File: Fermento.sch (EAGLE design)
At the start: 27 parts, among them Q1 32.768kHz, Q2 P-MOSFET

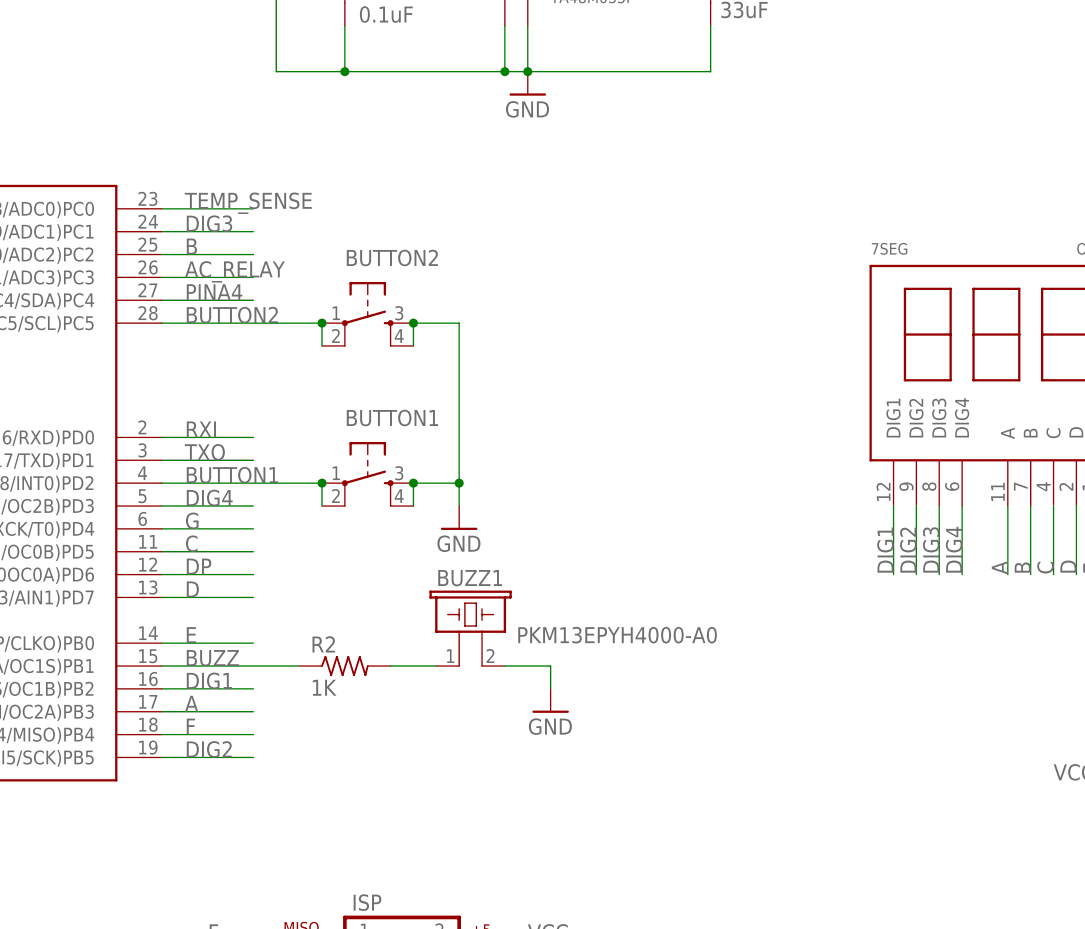
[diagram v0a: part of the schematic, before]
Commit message: Added firmware to the repo.
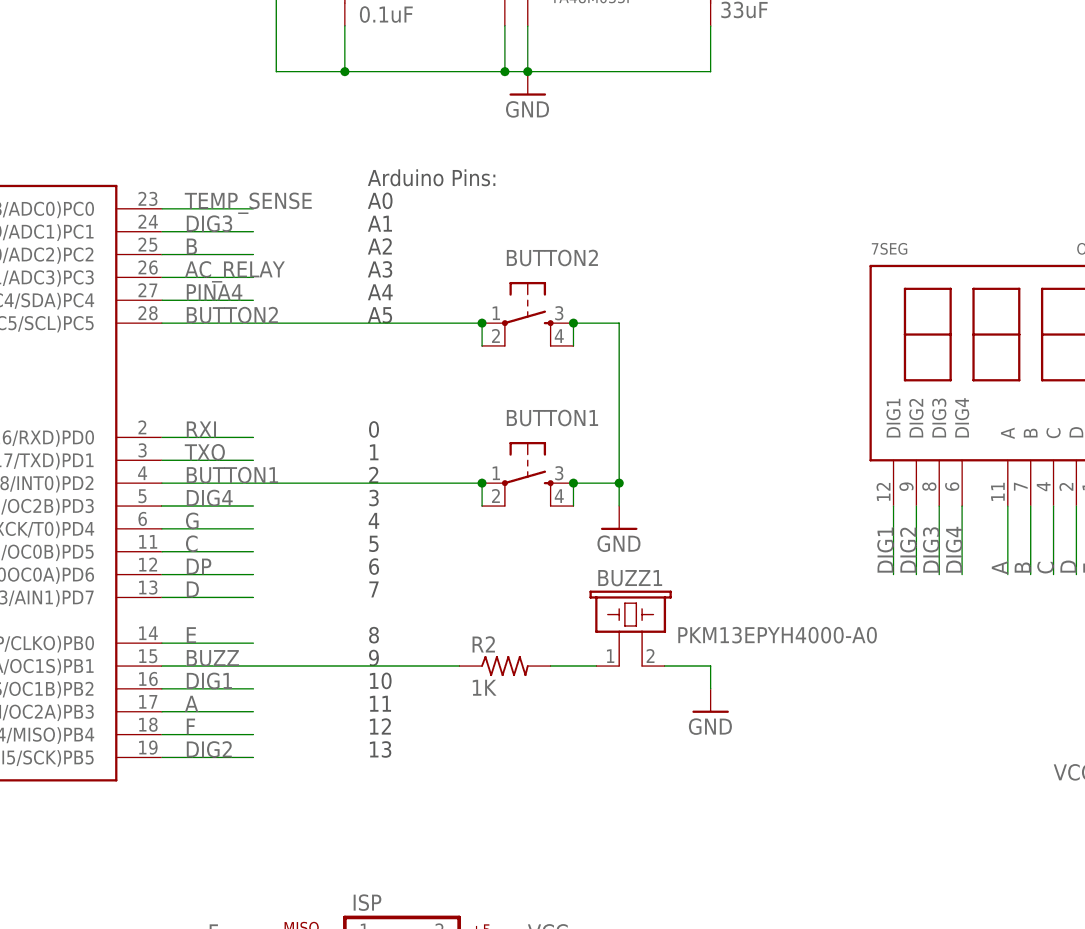
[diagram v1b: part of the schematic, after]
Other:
- note added: "0"
- note added: "1"
- note added: "10"
- note added: "11"
- note added: "12"
- note added: "13"
- note added: "3"
- note added: "4"
- note added: "5"
- note added: "6"
- note added: "7"
- note added: "8"
- note added: "9"
- note added: "A0"
- note added: "A1"
- note added: "A2"
- note added: "A3"
- note added: "A4"
- note added: "A5"
- note added: "Arduino Pins:"
- moved on the sheet: BUTTON1, BUTTON2, BUZZ1, R2
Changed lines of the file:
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@@
 <text x="259.08" y="-198.12" size="2.286" layer="94">2</text>
 <text x="190.5" y="-198.12" size="2.286" layer="94">based on BigTime by SparkFun</text>
+<text x="137.16" y="-81.28" size="1.778" layer="97">0</text>
+<text x="137.16" y="-83.82" size="1.778" layer="97">1</text>
+<text x="137.16" y="-86.36" size="1.778" layer="97">2</text>
+<text x="137.16" y="-88.9" size="1.778" layer="97">3</text>
+<text x="137.16" y="-91.44" size="1.778" layer="97">4</text>
+<text x="137.16" y="-93.98" size="1.778" layer="97">5</text>
+<text x="137.16" y="-96.52" size="1.778" layer="97">6</text>
+<text x="137.16" y="-99.06" size="1.778" layer="97">7</text>
+<text x="137.16" y="-104.14" size="1.778" layer="97">8</text>
+<text x="137.16" y="-106.68" size="1.778" layer="97">9</text>
+<text x="137.16" y="-109.22" size="1.778" layer="97">10</text>
+<text x="137.16" y="-111.76" size="1.778" layer="97">11</text>
+<text x="137.16" y="-114.3" size="1.778" layer="97">12</text>
+<text x="137.16" y="-116.84" size="1.778" layer="97">13</text>
+<text x="137.16" y="-55.88" size="1.778" layer="97">A0</text>
+<text x="137.16" y="-58.42" size="1.778" layer="97">A1</text>
+<text x="137.16" y="-60.96" size="1.778" layer="97">A2</text>
+<text x="137.16" y="-63.5" size="1.778" layer="97">A3</text>
+<text x="137.16" y="-66.04" size="1.778" layer="97">A4</text>
+<text x="137.16" y="-68.58" size="1.778" layer="97">A5</text>
+<text x="137.16" y="-53.34" size="1.778" layer="97">Arduino Pins:</text>
 </plain>
 <instances>
@@
 <instance part="C2" gate="G$1" x="40.64" y="-99.06"/>
 <instance part="R1" gate="G$1" x="58.42" y="-43.18" rot="R90"/>
-<instance part="R2" gate="G$1" x="134.62" y="-106.68"/>
-<instance part="BUTTON1" gate="S" x="137.16" y="-86.36"/>
+<instance part="R2" gate="G$1" x="152.4" y="-106.68"/>
+<instance part="BUTTON1" gate="S" x="154.94" y="-86.36"/>
 <instance part="C3" gate="G$1" x="81.28" y="-38.1" rot="R270"/>
 <instance part="GND1" gate="1" x="40.64" y="-78.74"/>
 <instance part="GND2" gate="1" x="40.64" y="-109.22"/>
 <instance part="Q1" gate="G$1" x="53.34" y="-76.2" rot="R90"/>
-<instance part="BUZZ1" gate="G$1" x="147.32" y="-104.14"/>
+<instance part="BUZZ1" gate="G$1" x="165.1" y="-104.14"/>
 <instance part="TEMP1" gate="G$1" x="231.14" y="-25.4"/>
 <instance part="P+2" gate="1" x="40.64" y="-88.9"/>
-<instance part="GND3" gate="1" x="147.32" y="-91.44"/>
-<instance part="GND4" gate="1" x="157.48" y="-111.76"/>
+<instance part="GND3" gate="1" x="165.1" y="-91.44"/>
+<instance part="GND4" gate="1" x="175.26" y="-111.76"/>
 <instance part="P+3" gate="1" x="58.42" y="-27.94"/>
 <instance part="P+4" gate="1" x="223.52" y="-114.3"/>
@@
 <instance part="SERIAL" gate="A" x="93.98" y="-33.02"/>
 <instance part="EXTRA" gate="A" x="248.92" y="-129.54"/>
-<instance part="BUTTON2" gate="S" x="137.16" y="-68.58"/>
+<instance part="BUTTON2" gate="S" x="154.94" y="-68.58"/>
 <instance part="Q2" gate="G$1" x="53.34" y="-162.56"/>
 <instance part="P+1" gate="1" x="55.88" y="-149.86"/>
@@
 </segment>
 <segment>
-<wire x1="142.24" y1="-86.36" x2="147.32" y2="-86.36" width="0.1524" layer="91"/>
-<wire x1="147.32" y1="-86.36" x2="147.32" y2="-88.9" width="0.1524" layer="91"/>
+<wire x1="160.02" y1="-86.36" x2="165.1" y2="-86.36" width="0.1524" layer="91"/>
+<wire x1="165.1" y1="-86.36" x2="165.1" y2="-88.9" width="0.1524" layer="91"/>
 <pinref part="BUTTON1" gate="S" pin="3"/>
 <pinref part="GND3" gate="1" pin="GND"/>
-<junction x="147.32" y="-86.36"/>
+<junction x="165.1" y="-86.36"/>
 <pinref part="BUTTON2" gate="S" pin="3"/>
-<wire x1="142.24" y1="-68.58" x2="147.32" y2="-68.58" width="0.1524" layer="91"/>
-<wire x1="147.32" y1="-68.58" x2="147.32" y2="-86.36" width="0.1524" layer="91"/>
-<junction x="142.24" y="-68.58"/>
-<junction x="142.24" y="-86.36"/>
+<wire x1="160.02" y1="-68.58" x2="165.1" y2="-68.58" width="0.1524" layer="91"/>
+<wire x1="165.1" y1="-68.58" x2="165.1" y2="-86.36" width="0.1524" layer="91"/>
+<junction x="160.02" y="-68.58"/>
+<junction x="160.02" y="-86.36"/>
 <pinref part="BUTTON2" gate="S" pin="4"/>
-<wire x1="142.24" y1="-68.58" x2="142.24" y2="-71.12" width="0.1524" layer="91"/>
+<wire x1="160.02" y1="-68.58" x2="160.02" y2="-71.12" width="0.1524" layer="91"/>
 <pinref part="BUTTON1" gate="S" pin="4"/>
-<wire x1="142.24" y1="-86.36" x2="142.24" y2="-88.9" width="0.1524" layer="91"/>
-</segment>
-<segment>
-<wire x1="152.4" y1="-106.68" x2="157.48" y2="-106.68" width="0.1524" layer="91"/>
-<wire x1="157.48" y1="-106.68" x2="157.48" y2="-109.22" width="0.1524" layer="91"/>
+<wire x1="160.02" y1="-86.36" x2="160.02" y2="-88.9" width="0.1524" layer="91"/>
+</segment>
+<segment>
+<wire x1="170.18" y1="-106.68" x2="175.26" y2="-106.68" width="0.1524" layer="91"/>
+<wire x1="175.26" y1="-106.68" x2="175.26" y2="-109.22" width="0.1524" layer="91"/>
 <pinref part="BUZZ1" gate="G$1" pin="2"/>
 <pinref part="GND4" gate="1" pin="GND"/>
@@
 <net name="BUZZ" class="0">
 <segment>
-<wire x1="114.3" y1="-106.68" x2="129.54" y2="-106.68" width="0.1524" layer="91"/>
+<wire x1="114.3" y1="-106.68" x2="147.32" y2="-106.68" width="0.1524" layer="91"/>
 <label x="116.84" y="-106.68" size="1.778" layer="95"/>
 <pinref part="ATMEGA328" gate="G$1" pin="(PCI1/OC1A/OC1S)PB1"/>
@@
 <net name="N$13" class="0">
 <segment>
-<wire x1="139.7" y1="-106.68" x2="144.78" y2="-106.68" width="0.1524" layer="91"/>
+<wire x1="157.48" y1="-106.68" x2="162.56" y2="-106.68" width="0.1524" layer="91"/>
 <pinref part="R2" gate="G$1" pin="2"/>
 <pinref part="BUZZ1" gate="G$1" pin="1"/>
@@
 <net name="BUTTON1" class="0">
 <segment>
-<wire x1="114.3" y1="-86.36" x2="132.08" y2="-86.36" width="0.1524" layer="91"/>
+<wire x1="114.3" y1="-86.36" x2="149.86" y2="-86.36" width="0.1524" layer="91"/>
 <label x="116.84" y="-86.36" size="1.778" layer="95"/>
 <pinref part="ATMEGA328" gate="G$1" pin="(PCI18/INT0)PD2"/>
 <pinref part="BUTTON1" gate="S" pin="1"/>
-<junction x="132.08" y="-86.36"/>
+<junction x="149.86" y="-86.36"/>
 <pinref part="BUTTON1" gate="S" pin="2"/>
-<wire x1="132.08" y1="-86.36" x2="132.08" y2="-88.9" width="0.1524" layer="91"/>
+<wire x1="149.86" y1="-86.36" x2="149.86" y2="-88.9" width="0.1524" layer="91"/>
 </segment>
 <segment>
@@
 <net name="BUTTON2" class="0">
 <segment>
-<wire x1="114.3" y1="-68.58" x2="132.08" y2="-68.58" width="0.1524" layer="91"/>
+<wire x1="114.3" y1="-68.58" x2="149.86" y2="-68.58" width="0.1524" layer="91"/>
 <label x="116.84" y="-68.58" size="1.778" layer="95"/>
 <pinref part="ATMEGA328" gate="G$1" pin="(PCI13/ADC5/SCL)PC5"/>
 <pinref part="BUTTON2" gate="S" pin="1"/>
-<junction x="132.08" y="-68.58"/>
+<junction x="149.86" y="-68.58"/>
 <pinref part="BUTTON2" gate="S" pin="2"/>
-<wire x1="132.08" y1="-68.58" x2="132.08" y2="-71.12" width="0.1524" layer="91"/>
-</segment>
-<segment>
+<wire x1="149.86" y1="-68.58" x2="149.86" y2="-71.12" width="0.1524" layer="91"/>
+</segment>
+<segment>
